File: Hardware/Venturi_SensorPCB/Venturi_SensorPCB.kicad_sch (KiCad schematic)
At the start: 60 parts, among them IC1 ADS7961SDBT, J1 Sensor-PCB, Q1 BSS138, Q2 BSS138, U1 QRE1113GR, U10 QRE1113GR, U11 QRE1113GR, U12 QRE1113GR, U13 QRE1113GR, U14 QRE1113GR, U15 QRE1113GR, U16 QRE1113GR, U2 QRE1113GR, U3 QRE1113GR, U4 QRE1113GR, U5 QRE1113GR, U6 QRE1113GR, U7 QRE1113GR, U8 QRE1113GR, U9 QRE1113GR

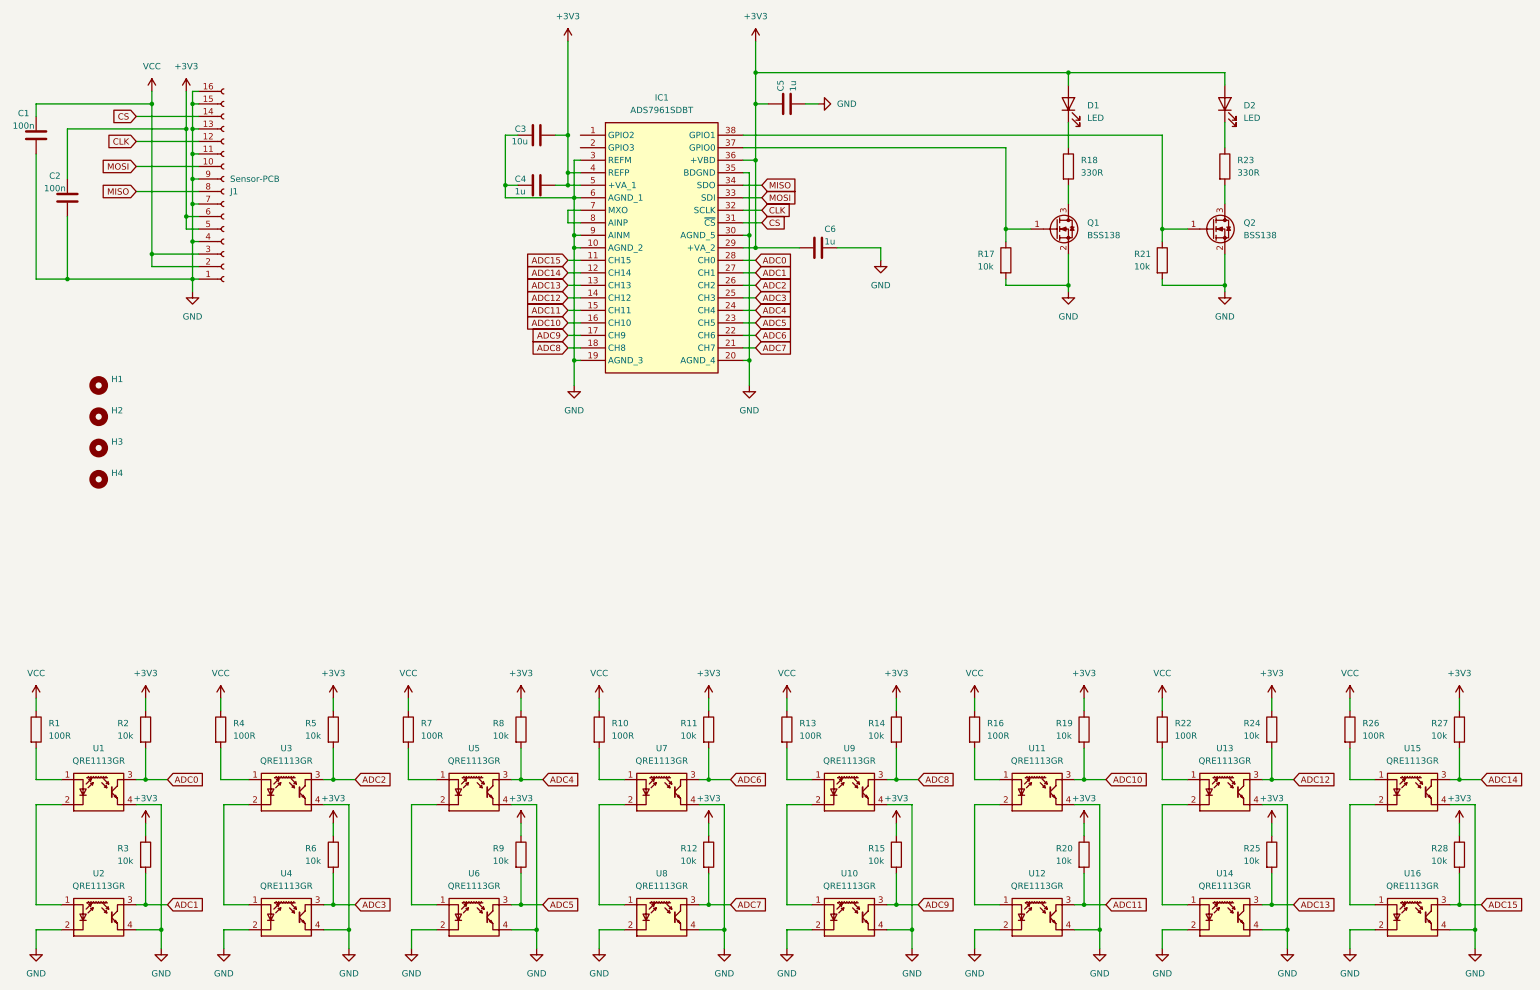
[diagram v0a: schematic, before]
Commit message: Updated PCB-Design for 20MHz SPI speed
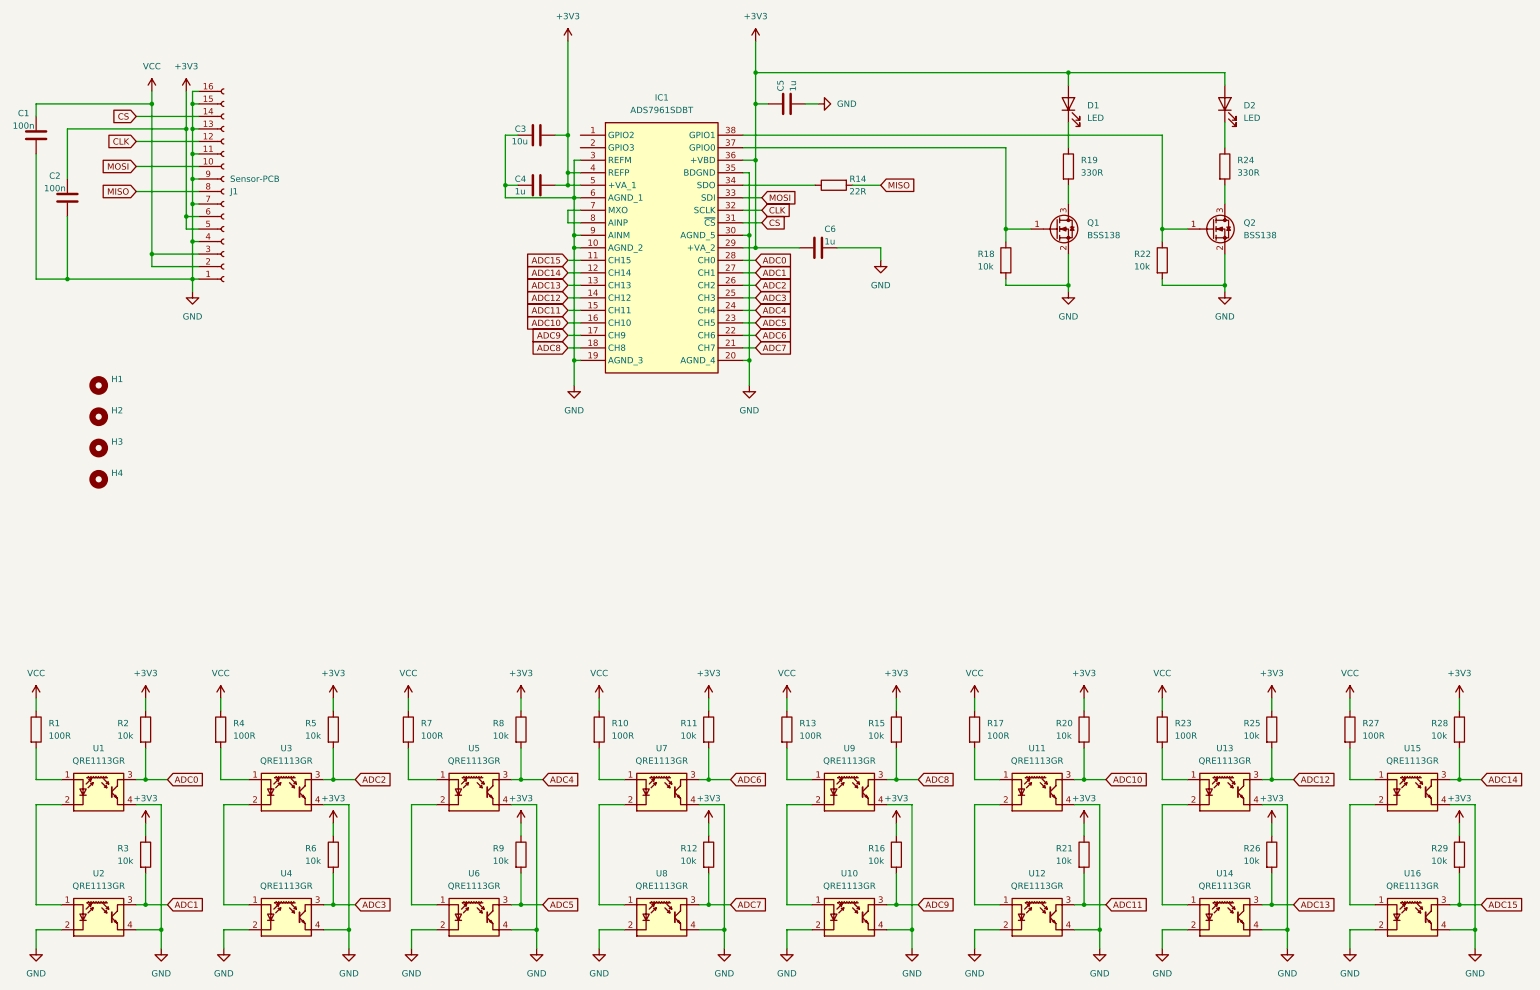
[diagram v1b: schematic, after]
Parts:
- added R14: 22R, Resistor_SMD:R_0805_2012Metric_Pad1.20x1.40mm_HandSolder, symbol Device:R
- renumbered R14 to R15, R15 to R16, R16 to R17, R17 to R18, R18 to R19, R19 to R20, R20 to R21, R21 to R22, R22 to R23, R23 to R24, R24 to R25, R25 to R26, R26 to R27, R27 to R28, R28 to R29
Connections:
- net MISO: now also R14.2; no longer IC1.34 (SDO)
- new net: IC1.34 (SDO), R14.1
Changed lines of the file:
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@@
 	(wire
 		(pts
+			(xy 184.785 48.26) (xy 190.5 48.26)
+		)
+		(stroke
+			(width 0)
+			(type default)
+		)
+	)
+	(wire
+		(pts
 			(xy 39.37 173.99) (xy 44.45 173.99)
 		)
@@
 	(wire
 		(pts
-			(xy 162.56 48.26) (xy 166.37 48.26)
+			(xy 162.56 48.26) (xy 177.165 48.26)
 		)
 		(stroke
@@
 	(global_label "MISO"
 		(shape input)
-		(at 166.37 48.26 0)
+		(at 190.5 48.26 0)
 		(fields_autoplaced yes)
 		(effects
@@
 		)
 		(property "Intersheetrefs" "${INTERSHEET_REFS}"
-			(at 173.9514 48.26 0)
+			(at 198.0814 48.26 0)
 			(hide yes)
 			(show_name no)
@@
 		(in_pos_files yes)
 		(dnp no)
-		(property "Reference" "R19"
+		(property "Reference" "R20"
 			(at 226.06 157.48 0)
 			(show_name no)
@@
 			(project "Venturi_SensorPCB"
 				(path "/179da9ab-1703-43d9-a037-538492c203c2"
-					(reference "R19")
+					(reference "R20")
 					(unit 1)
 				)
@@
 		(dnp no)
 		(fields_autoplaced yes)
-		(property "Reference" "R26"
+		(property "Reference" "R27"
 			(at 288.29 157.4799 0)
 			(show_name no)
@@
 			(project "Venturi_SensorPCB"
 				(path "/179da9ab-1703-43d9-a037-538492c203c2"
-					(reference "R26")
+					(reference "R27")
 					(unit 1)
 				)
@@
 		(in_pos_files yes)
 		(dnp no)
-		(property "Reference" "R20"
+		(property "Reference" "R21"
 			(at 226.06 182.88 0)
 			(show_name no)
@@
 			(project "Venturi_SensorPCB"
 				(path "/179da9ab-1703-43d9-a037-538492c203c2"
-					(reference "R20")
+					(reference "R21")
 					(unit 1)
 				)
@@
 		(in_pos_files yes)
 		(dnp no)
-		(property "Reference" "R27"
+		(property "Reference" "R28"
 			(at 302.26 157.48 0)
 			(show_name no)
@@
 			(project "Venturi_SensorPCB"
 				(path "/179da9ab-1703-43d9-a037-538492c203c2"
-					(reference "R27")
+					(reference "R28")
 					(unit 1)
 				)
@@
 		(in_pos_files yes)
 		(dnp no)
-		(property "Reference" "R24"
+		(property "Reference" "R25"
 			(at 264.16 157.48 0)
 			(show_name no)
@@
 			(project "Venturi_SensorPCB"
 				(path "/179da9ab-1703-43d9-a037-538492c203c2"
-					(reference "R24")
+					(reference "R25")
 					(unit 1)
 				)
@@
 		(in_pos_files yes)
 		(dnp no)
-		(property "Reference" "R21"
+		(property "Reference" "R22"
 			(at 241.935 62.23 0)
 			(show_name no)
@@
 			(project "Venturi_SensorPCB"
 				(path "/179da9ab-1703-43d9-a037-538492c203c2"
-					(reference "R21")
+					(reference "R22")
 					(unit 1)
 				)
@@
 		(in_pos_files yes)
 		(dnp no)
-		(property "Reference" "R14"
+		(property "Reference" "R15"
 			(at 187.96 157.48 0)
 			(show_name no)
@@
 			(project "Venturi_SensorPCB"
 				(path "/179da9ab-1703-43d9-a037-538492c203c2"
-					(reference "R14")
+					(reference "R15")
 					(unit 1)
 				)
@@
 		(dnp no)
 		(fields_autoplaced yes)
-		(property "Reference" "R23"
+		(property "Reference" "R24"
 			(at 262.89 43.1799 0)
 			(show_name no)
@@
 			(project "Venturi_SensorPCB"
 				(path "/179da9ab-1703-43d9-a037-538492c203c2"
-					(reference "R23")
+					(reference "R24")
 					(unit 1)
 				)
@@
 		(dnp no)
 		(fields_autoplaced yes)
-		(property "Reference" "R16"
+		(property "Reference" "R17"
 			(at 212.09 157.4799 0)
 			(show_name no)
@@
 			(project "Venturi_SensorPCB"
 				(path "/179da9ab-1703-43d9-a037-538492c203c2"
-					(reference "R16")
+					(reference "R17")
 					(unit 1)
 				)
@@
 		(in_pos_files yes)
 		(dnp no)
-		(property "Reference" "R15"
+		(property "Reference" "R16"
 			(at 187.96 182.88 0)
 			(show_name no)
@@
 			(project "Venturi_SensorPCB"
 				(path "/179da9ab-1703-43d9-a037-538492c203c2"
-					(reference "R15")
+					(reference "R16")
 					(unit 1)
 				)
@@
 		(in_pos_files yes)
 		(dnp no)
-		(property "Reference" "R17"
+		(property "Reference" "R18"
 			(at 210.185 62.23 0)
 			(show_name no)
@@
 			(project "Venturi_SensorPCB"
 				(path "/179da9ab-1703-43d9-a037-538492c203c2"
-					(reference "R17")
+					(reference "R18")
 					(unit 1)
 				)
@@
 		(in_pos_files yes)
 		(dnp no)
-		(property "Reference" "R28"
+		(property "Reference" "R29"
 			(at 302.26 182.88 0)
 			(show_name no)
@@
 			(project "Venturi_SensorPCB"
 				(path "/179da9ab-1703-43d9-a037-538492c203c2"
-					(reference "R28")
+					(reference "R29")
 					(unit 1)
 				)
@@
 		(in_pos_files yes)
 		(dnp no)
-		(property "Reference" "R25"
+		(property "Reference" "R26"
 			(at 264.16 182.88 0)
 			(show_name no)
@@
 			(project "Venturi_SensorPCB"
 				(path "/179da9ab-1703-43d9-a037-538492c203c2"
-					(reference "R25")
+					(reference "R26")
+					(unit 1)
+				)
+			)
+		)
+	)
+	(symbol
+		(lib_id "Device:R")
+		(at 180.975 48.26 90)
+		(mirror x)
+		(unit 1)
+		(body_style 1)
+		(exclude_from_sim no)
+		(in_bom yes)
+		(on_board yes)
+		(in_pos_files yes)
+		(dnp no)
+		(property "Reference" "R14"
+			(at 184.15 46.99 90)
+			(show_name no)
+			(do_not_autoplace no)
+			(effects
+				(font
+					(size 1.27 1.27)
+				)
+				(justify right)
+			)
+		)
+		(property "Value" "22R"
+			(at 184.15 49.53 90)
+			(show_name no)
+			(do_not_autoplace no)
+			(effects
+				(font
+					(size 1.27 1.27)
+				)
+				(justify right)
+			)
+		)
+		(property "Footprint" "Resistor_SMD:R_0805_2012Metric_Pad1.20x1.40mm_HandSolder"
+			(at 180.975 46.482 90)
+			(hide yes)
+			(show_name no)
+			(do_not_autoplace no)
+			(effects
+				(font
+					(size 1.27 1.27)
+				)
+			)
+		)
+		(property "Datasheet" ""
+			(at 180.975 48.26 0)
+			(hide yes)
+			(show_name no)
+			(do_not_autoplace no)
+			(effects
+				(font
+					(size 1.27 1.27)
+				)
+			)
+		)
+		(property "Description" "Resistor"
+			(at 180.975 48.26 0)
+			(hide yes)
+			(show_name no)
+			(do_not_autoplace no)
+			(effects
+				(font
+					(size 1.27 1.27)
+				)
+			)
+		)
+		(pin "2"
+		)
+		(pin "1"
+		)
+		(instances
+			(project "Venturi_SensorPCB"
+				(path "/179da9ab-1703-43d9-a037-538492c203c2"
+					(reference "R14")
 					(unit 1)
 				)
@@
 		(dnp no)
 		(fields_autoplaced yes)
-		(property "Reference" "R18"
+		(property "Reference" "R19"
 			(at 231.14 43.1799 0)
 			(show_name no)
@@
 			(project "Venturi_SensorPCB"
 				(path "/179da9ab-1703-43d9-a037-538492c203c2"
-					(reference "R18")
+					(reference "R19")
 					(unit 1)
 				)
@@
 		(dnp no)
 		(fields_autoplaced yes)
-		(property "Reference" "R22"
+		(property "Reference" "R23"
 			(at 250.19 157.4799 0)
 			(show_name no)
@@
 			(project "Venturi_SensorPCB"
 				(path "/179da9ab-1703-43d9-a037-538492c203c2"
-					(reference "R22")
+					(reference "R23")
 					(unit 1)
 				)
